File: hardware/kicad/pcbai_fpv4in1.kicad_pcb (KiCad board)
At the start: 2 copper layers, 230 parts, among them J13 AT32F421K8T7, J18 AT32F421K8T7, J2 LMR51420YDDCR, J23 AT32F421K8T7, J4 SM08B-SRSS-TB, J5 USBLC6-2SC6, J6 USBLC6-2SC6, J7 USBLC6-2SC6, J8 AT32F421K8T7, Q1 AON6260, Q10 AON6260, Q11 AON6260, Q12 AON6260, Q13 AON6260, Q14 AON6260, Q15 AON6260, Q16 AON6260, Q17 AON6260, Q18 AON6260, Q19 AON6260, Q2 AON6260, Q20 AON6260, Q21 AON6260, Q22 AON6260, Q23 AON6260, Q24 AON6260, Q25 AON6260, Q26 AON6260, Q27 AON6260, Q28 AON6260, Q3 AON6260, Q4 AON6260, Q5 AON6260, Q6 AON6260, Q7 AON6260, Q8 AON6260, Q9 AON6260

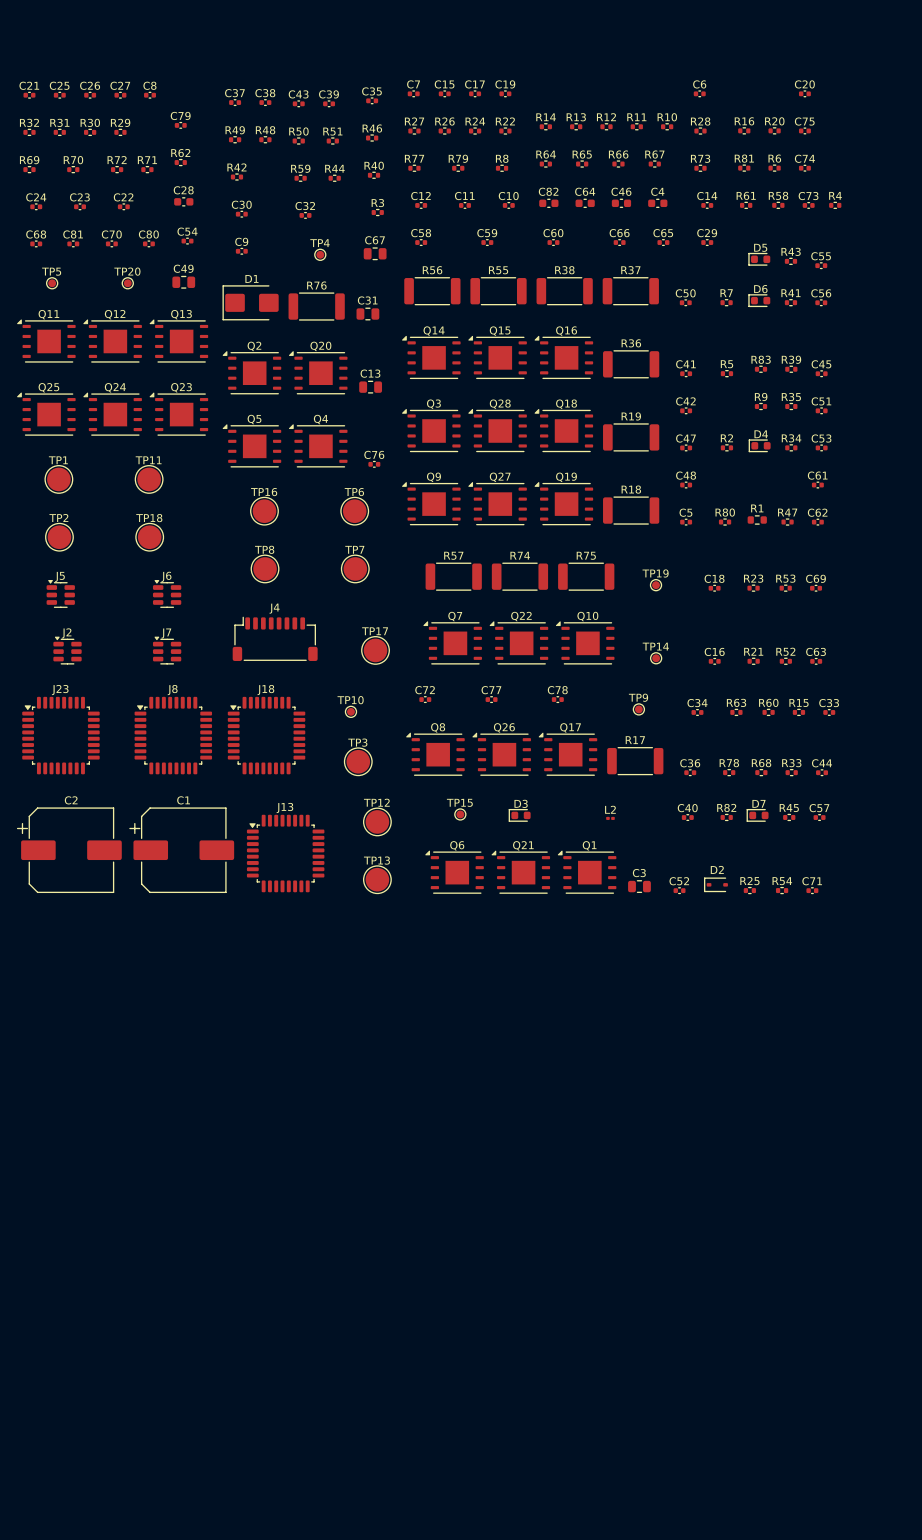
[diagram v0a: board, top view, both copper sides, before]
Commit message: Phase 4a: footprint typos fixed + 6-layer stack + Edge.Cuts + M3 holes
Five footprint typos from Phase 3c fixed at the SKiDL .py source per
Rigor §10 (every name verified against actual KiCad std-lib pretty
directory listings):

  L_1608_0603Metric → L_0603_1608Metric (axis-order swap)
  SC-70-6_Handsoldering → SOT-363_SC-70-6 (JEDEC prefix + drop suffix)
  TerminalBlock_Phoenix_MPT-2.54mm_1x02 → PinHeader_1x02_P2.54mm_Vertical
    (KiCad has no Phoenix MPT 2.54mm; simpler 2-pin pad for BATT)
  VQFN-24_4x4mm → HVQFN-24-1EP_4x4mm_P0.5mm_EP2.6x2.6mm (KiCad prefix)
  WSON-6-1EP EP0.9x1.6 → EP1x1.6 (KiCad's actual EP dimension)

Re-ran SKiDL + kinet2pcb: 249/249 footprints resolved, 0 missing.

Board setup (via hardware/kicad/setup_board.py — committed for repro):

  6-layer stack-up per PCB_PLAYBOOK §Routing + master's function map:
    F.Cu  — signal-side (MCUs + drivers + CSAs + decoupling + ...)
    In1.Cu — +VMOTOR power plane
    In2.Cu — GND plane
    In3.Cu — GND plane (redundant for return-path integrity)
    In4.Cu — +5V/+3V3 split plane
    B.Cu  — power-side (24+4 MOSFETs + shunts + bulk + heatsink)

  Edge.Cuts outline: 50.0 × 50.0 mm square (4× gr_line on Edge.Cuts).

  4× M3 mounting holes on 40 × 40 mm Betaflight pattern at corners
    (5,5), (45,5), (5,45), (45,45). 3.2 mm clearance dia, 6.0 mm pad.

Verification:
  kicad-cli pcb export svg succeeds (462 KB SVG output) → .kicad_pcb
  file loads cleanly in KiCad 9.

Phase 4b handoff: hardware/kicad/pcbai_fpv4in1.kicad_pcb is ready;
all 249 footprints currently at origin. Phase 4b places them per
sims/phase2_5_fit/placement_*.png reference.

REQUIREMENTS.md §Mechanical: 6-layer stack-up function table +
Edge.Cuts outline + mounting pattern locked.

Co-Authored-By: Claude Opus 4.7 (1M context) <noreply@anthropic.com>
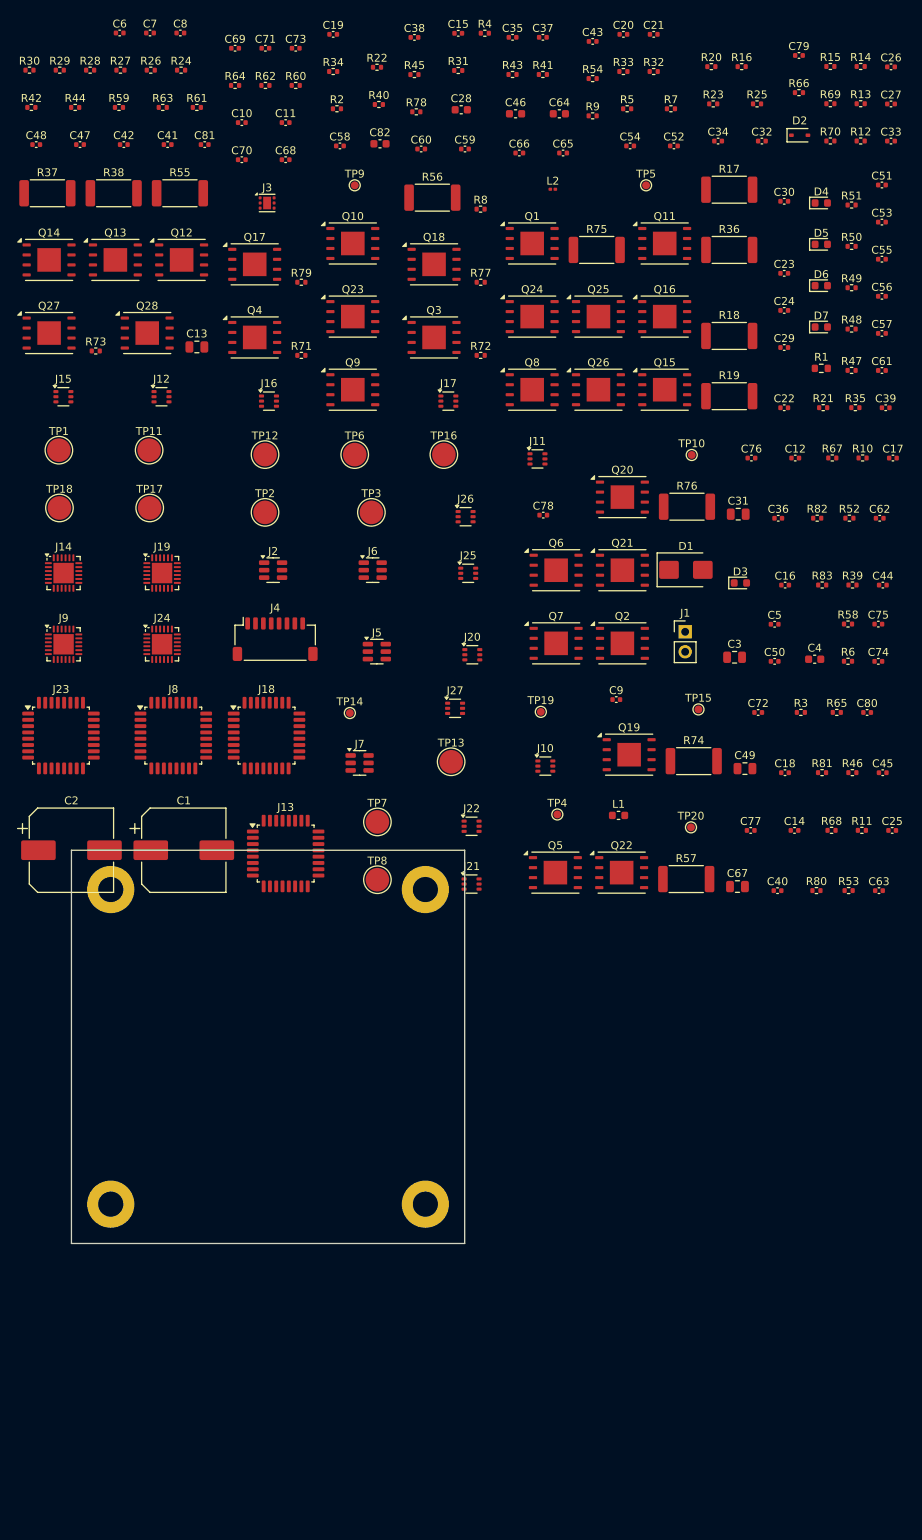
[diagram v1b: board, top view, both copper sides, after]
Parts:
- added ?: , MountingHole:MountingHole_3.2mm_M3, F.Cu at (5.00, 5.00)
- added ?: , MountingHole:MountingHole_3.2mm_M3, F.Cu at (45.0, 5.00)
- added ?: , MountingHole:MountingHole_3.2mm_M3, F.Cu at (5.00, 45.0)
- added ?: , MountingHole:MountingHole_3.2mm_M3, F.Cu at (45.0, 45.0)
- added J1: BATT_PAD, Connector_PinHeader_2.54mm:PinHeader_1x02_P2.54mm_Vertical, F.Cu at (78.0, -27.8)
- added J10: INA186A3IDCKR, Package_TO_SOT_SMD:SOT-363_SC-70-6, F.Cu at (60.3, -10.7)
- added J11: INA186A3IDCKR, Package_TO_SOT_SMD:SOT-363_SC-70-6, F.Cu at (59.3, -49.8)
- added J12: INA186A3IDCKR, Package_TO_SOT_SMD:SOT-363_SC-70-6, F.Cu at (11.5, -57.7)
- added J14: DRV8300DRGER, Package_DFN_QFN:HVQFN-24-1EP_4x4mm_P0.5mm_EP2.6x2.6mm, F.Cu at (-1.00, -35.2)
- added J15: INA186A3IDCKR, Package_TO_SOT_SMD:SOT-363_SC-70-6, F.Cu at (-1.02, -57.7)
- added J16: INA186A3IDCKR, Package_TO_SOT_SMD:SOT-363_SC-70-6, F.Cu at (25.1, -57.1)
- added J17: INA186A3IDCKR, Package_TO_SOT_SMD:SOT-363_SC-70-6, F.Cu at (47.9, -57.1)
- added J19: DRV8300DRGER, Package_DFN_QFN:HVQFN-24-1EP_4x4mm_P0.5mm_EP2.6x2.6mm, F.Cu at (11.5, -35.2)
- added J20: INA186A3IDCKR, Package_TO_SOT_SMD:SOT-363_SC-70-6, F.Cu at (51.0, -24.9)
- added J21: INA186A3IDCKR, Package_TO_SOT_SMD:SOT-363_SC-70-6, F.Cu at (50.9, 4.30)
- added J22: INA186A3IDCKR, Package_TO_SOT_SMD:SOT-363_SC-70-6, F.Cu at (50.9, -3.05)
- added J24: DRV8300DRGER, Package_DFN_QFN:HVQFN-24-1EP_4x4mm_P0.5mm_EP2.6x2.6mm, F.Cu at (11.5, -26.2)
- added J25: INA186A3IDCKR, Package_TO_SOT_SMD:SOT-363_SC-70-6, F.Cu at (50.4, -35.2)
- added J26: INA186A3IDCKR, Package_TO_SOT_SMD:SOT-363_SC-70-6, F.Cu at (50.1, -42.4)
- added J27: INA186A3IDCKR, Package_TO_SOT_SMD:SOT-363_SC-70-6, F.Cu at (48.8, -18.0)
- added J3: TLV76733DRVR, Package_SON:WSON-6-1EP_2x2mm_P0.65mm_EP1x1.6mm, F.Cu at (24.9, -82.3)
- added J9: DRV8300DRGER, Package_DFN_QFN:HVQFN-24-1EP_4x4mm_P0.5mm_EP2.6x2.6mm, F.Cu at (-1.00, -26.2)
- added L1: 0.47uH, Inductor_SMD:L_0603_1608Metric, F.Cu at (69.6, -4.43)
- moved C25 141.2 mm to (104.4, -2.52)
- moved C71 127.7 mm to (24.7, -102.0)
- moved C80 109.0 mm to (101.2, -17.5)
- moved R54 106.0 mm to (66.3, -98.1)
- moved R63 106.0 mm to (11.6, -94.4)
- moved R45 105.8 mm to (43.6, -98.6)
- moved R69 102.2 mm to (96.5, -94.9)
- moved C26 101.9 mm to (104.2, -99.6)
- moved R46 101.2 mm to (99.3, -9.87)
- moved C69 100.8 mm to (20.8, -102.0)
- moved R25 100.0 mm to (87.2, -94.9)
- moved R60 99.8 mm to (28.5, -97.2)
- moved TP20 99.6 mm to (78.8, -2.91)
- moved C27 98.0 mm to (104.2, -94.9)
- moved R70 96.3 mm to (96.5, -90.2)
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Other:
- board outline added: 50 x 50 mm
- copper layers 2 -> 6

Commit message: Phase 4b: scripted placement of 249 footprints per Phase 2.5 sketch
Authors hardware/kicad/scripts/place_board.py — idempotent script that
parses the .kicad_pcb (kinet2pcb output, all parts at origin), categorizes
footprints by value+ref, and assigns positions per the Phase 2.5
placement_sketch.py reference. Re-runnable.

Categorization by value/ref:
  - 24× AON6260 phase MOSFETs → 6×4 grid on B.Cu (heatsink zone center)
  - 4× AON6260 reverse-pol FETs (Q1-Q4) → B.Cu bottom row
  - 12× 0.2mΩ shunts → row above MOSFETs on B.Cu
  - 2× 470µF bulk caps → B.Cu left + right edges
  - 1× SMBJ33A TVS + 1× battery pad → B.Cu input zone
  - 4× AT32F421 MCUs → F.Cu corners (3,3), (38,3), (3,32), (38,32)
  - 4× DRV8300 drivers → adjacent to each MCU
  - 12× INA186 CSAs → clustered 3 per channel
  - LMR51420 buck + TLV76733 LDO + buck inductor + VDDA ferrite → F.Cu right side
  - 1× JST FC connector → F.Cu top center (T7 edge-accessible)
  - 3× USBLC6-2SC6 ESD → row near FC
  - 5× LEDs (1 PG + 4 status) + 12 motor pads (3 per edge × 4 channels per T7)
    + 8 SWD pads (left edge × 4 channels) — all distributed
  - ~156 per-channel passives (decoupling + BEMF dividers + bootstrap +
    status R) → 4× zones with 7×7 = 49-cell sub-grids per channel, 1.4 mm pitch

Verification (cross-checked via standalone Python):
  249 footprints total (excludes 4 mount holes which Phase 4a preserves)
  0 at origin ✓
  0 out of bounds (within 50×50 mm Edge.Cuts) ✓
  By layer: F.Cu 205 + B.Cu 44 ✓ (matches Phase 2.5 expected split)

T7 connector accessibility:
  FC connector at (21, 46) → top edge
  Battery pad at (8, 4) → bottom edge
  Motor pads at y=1, y=49, x=1, x=49 (one channel per edge)
  SWD pads at x=1 (left edge)
  All edge-accessible ✓

kicad-cli pcb export svg snapshots:
  sims/phase4b_placement/placement_F_Cu.svg (2.2 MB)
  sims/phase4b_placement/placement_B_Cu.svg (66 KB)

Phase 4c handoff: hardware/kicad/pcbai_fpv4in1.kicad_pcb has all 249
footprints placed. Phase 4c runs real Elmer 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
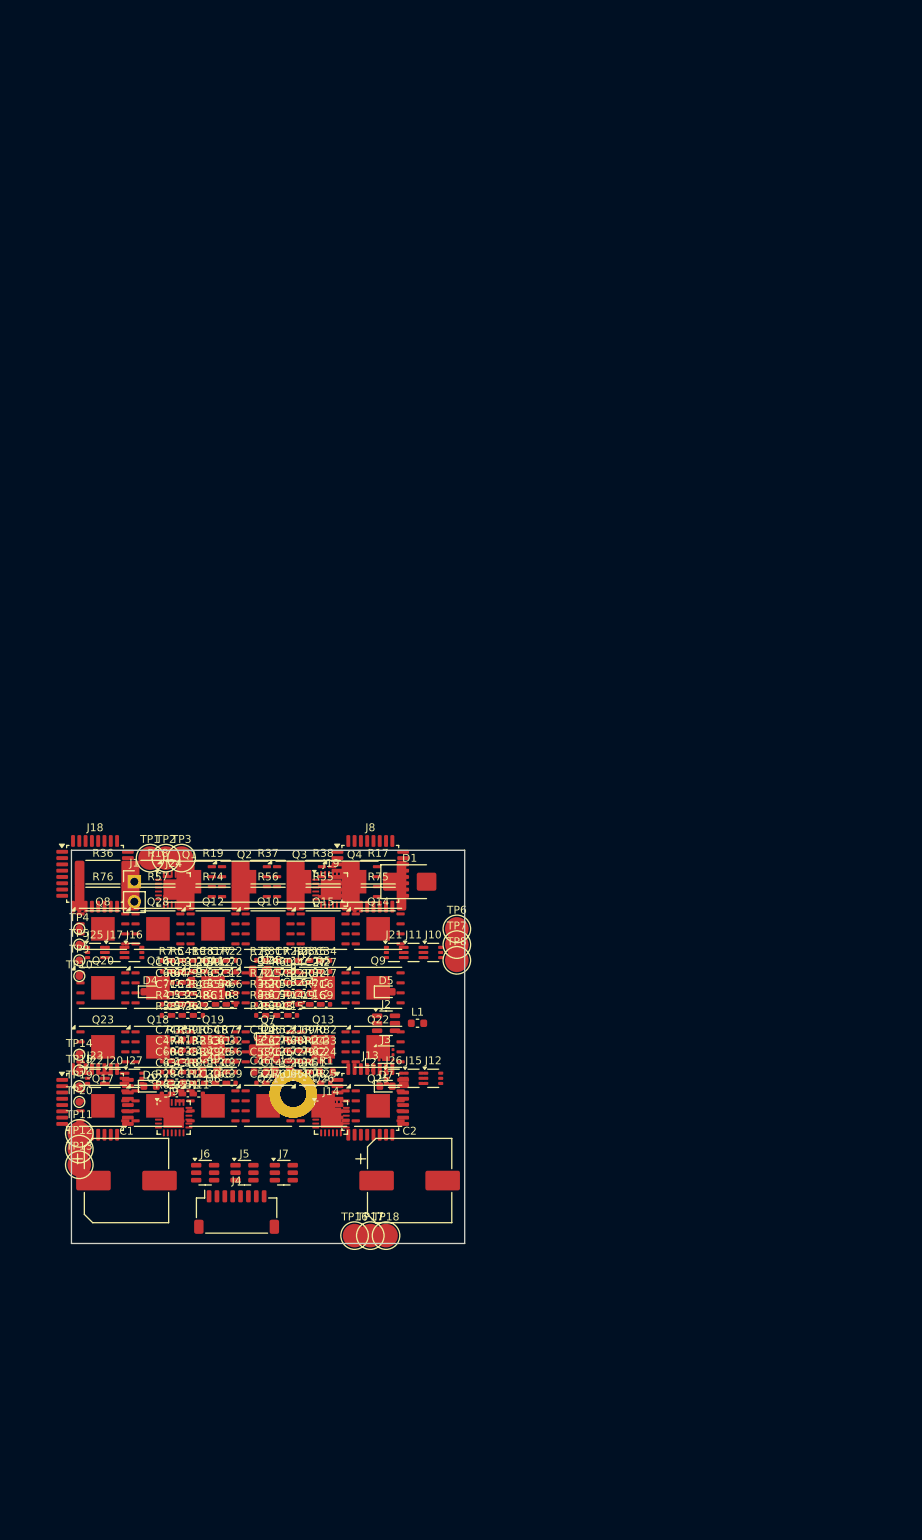
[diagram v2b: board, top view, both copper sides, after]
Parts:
- removed the ? at (5.00, 5.00)
- removed the ? at (45.0, 5.00)
- removed the ? at (5.00, 45.0)
- removed the ? at (45.0, 45.0)
- added ? (x4): , MountingHole:MountingHole_3.2mm_M3, F.Cu at (28.2, 31.0)
- C1, C2, D1, J1, Q1, Q10, Q11, Q12, Q13, Q14, Q15, Q16, Q17, Q18, Q19, Q2, Q20, Q21, Q22, Q23, Q24, Q25, Q26, Q27, Q28, Q3, Q4, Q5, Q6, Q7, Q8, Q9, R17, R18, R19, R36, R37, R38, R55, R56, R57, R74, R75, R76: moved to B.Cu
- moved C26 152.4 mm to (19.0, 26.8)
- moved R13 147.6 mm to (14.8, 25.4)
- moved C51 145.4 mm to (14.8, 31.0)
- moved C79 142.5 mm to (29.6, 26.8)
- moved C43 141.3 mm to (13.4, 28.2)
- moved C35 141.0 mm to (13.4, 31.0)
- moved R14 139.4 mm to (28.2, 19.6)
- moved C37 137.4 mm to (20.4, 28.2)
- moved R15 136.4 mm to (25.4, 16.8)
- moved C33 136.1 mm to (32.4, 25.4)
- moved R25 136.0 mm to (32.4, 29.6)
- moved R69 136.0 mm to (25.4, 21.0)
- moved C21 135.7 mm to (28.2, 24.0)
- moved R33 135.5 mm to (13.4, 24.0)
- moved R66 135.3 mm to (20.4, 18.2)
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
